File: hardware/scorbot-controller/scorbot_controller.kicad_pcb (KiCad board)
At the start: 2 copper layers, 185 x 128 mm, 102 parts, among them J1 12V in (CUI PJ-102AH, 2.1 mm), J2 12V in (screw terminal, +/-), J3 E-STOP (NC, in VM line), J4 DD-50 female R/A (robot cable), J5 I2C expansion, J6 Spare TCA9555 I/O, J7 FUSE alt: wire inline 5A fuse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, U1 DROK mini buck, set to 5V, U10 Pololu #4035 DRV8874 (M1), U11 Pololu #4035 DRV8874 (M2), U12 Pololu #4035 DRV8874 (M3), U13 Pololu #4035 DRV8874 (M4), U14 Pololu #4035 DRV8874 (M5), U15 Pololu #4035 DRV8874 (M6), U2 ESP32-DevKitC (WROOM-32D or -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, U5 TCA9555PWR (0x20), U6 ADS1115IDGSR (0x48), U7 ADS1115IDGSR (0x49)

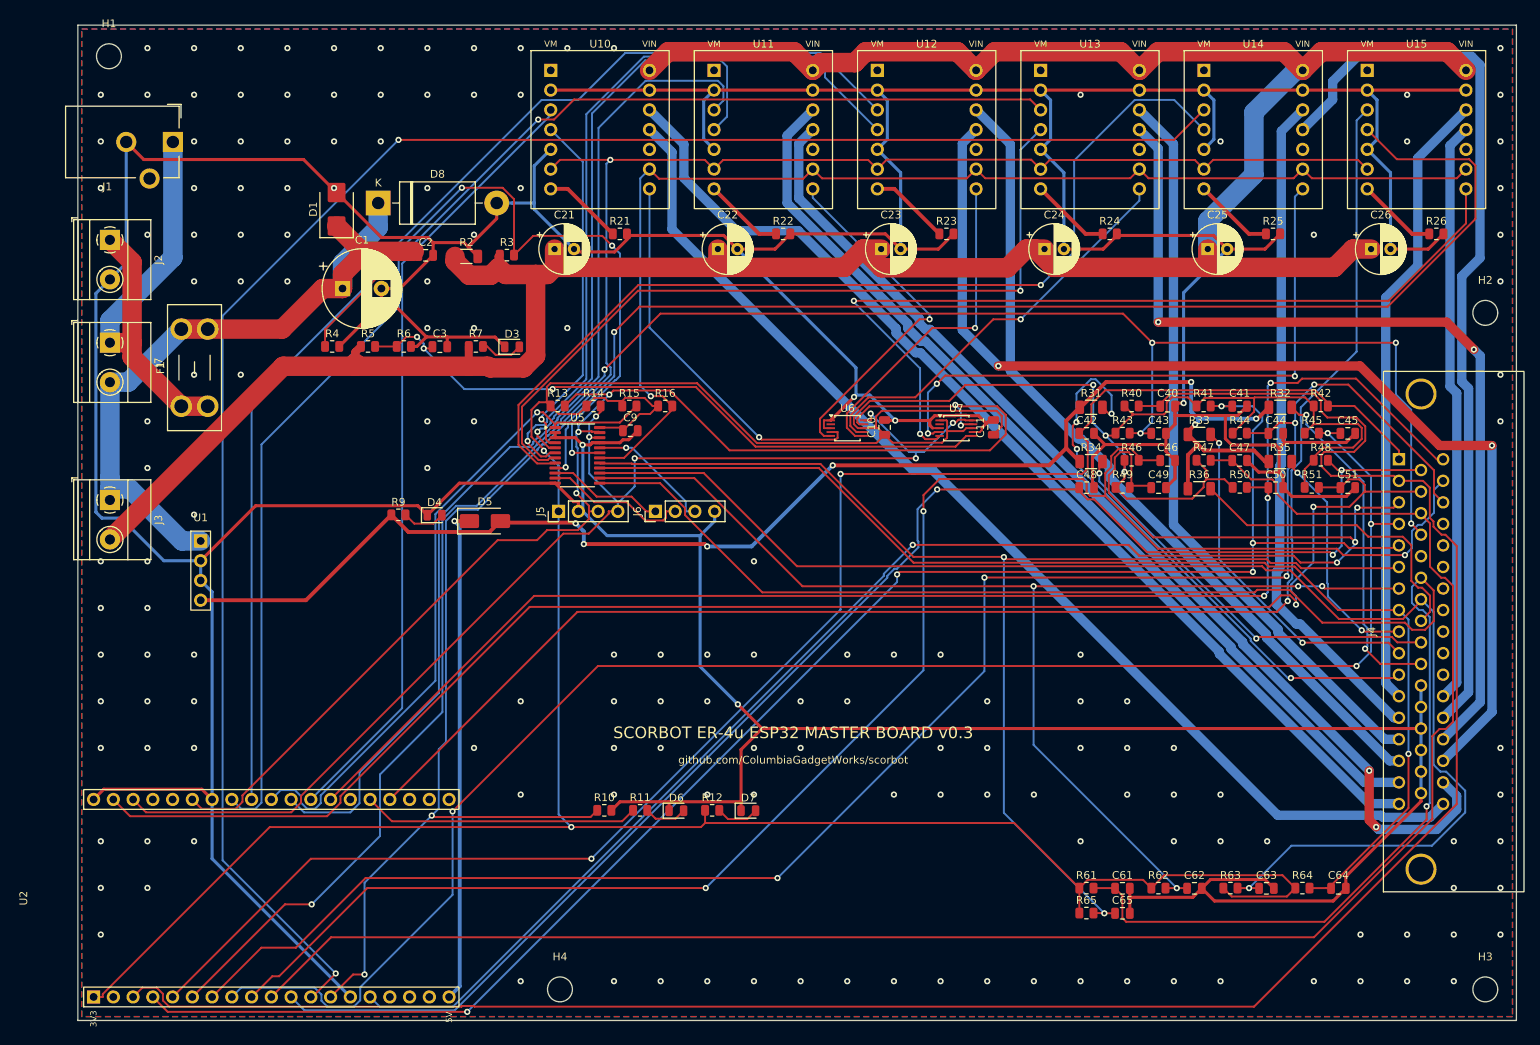
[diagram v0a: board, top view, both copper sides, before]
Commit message: v0.4: DD-50 footprint per Amphenol DD50S564TLF, logos on silkscreen, LCSC fixes
- DD-50: tail rows 2.54 mm apart, row 3 10.40 mm from the flange (Amphenol
  D-Sub brochure, termination type 5); bracket holes still to confirm
- Columbia Gadget Works logo on F.SilkS, Stealie on B.SilkS (silk_art.py)
- R31-R36 47R now 2512 1 W (~0.3 W each); D6 status LED red (C84256)
- Clear LCSC numbers that turned out wrong (TCA9555, 47R); previews draw silk on top

Co-Authored-By: Claude Opus 5.5 <noreply@anthropic.com>
Claude-Session: https://claude.ai/code/session_01EVE6PZ95cMufMkAr9pDFuN
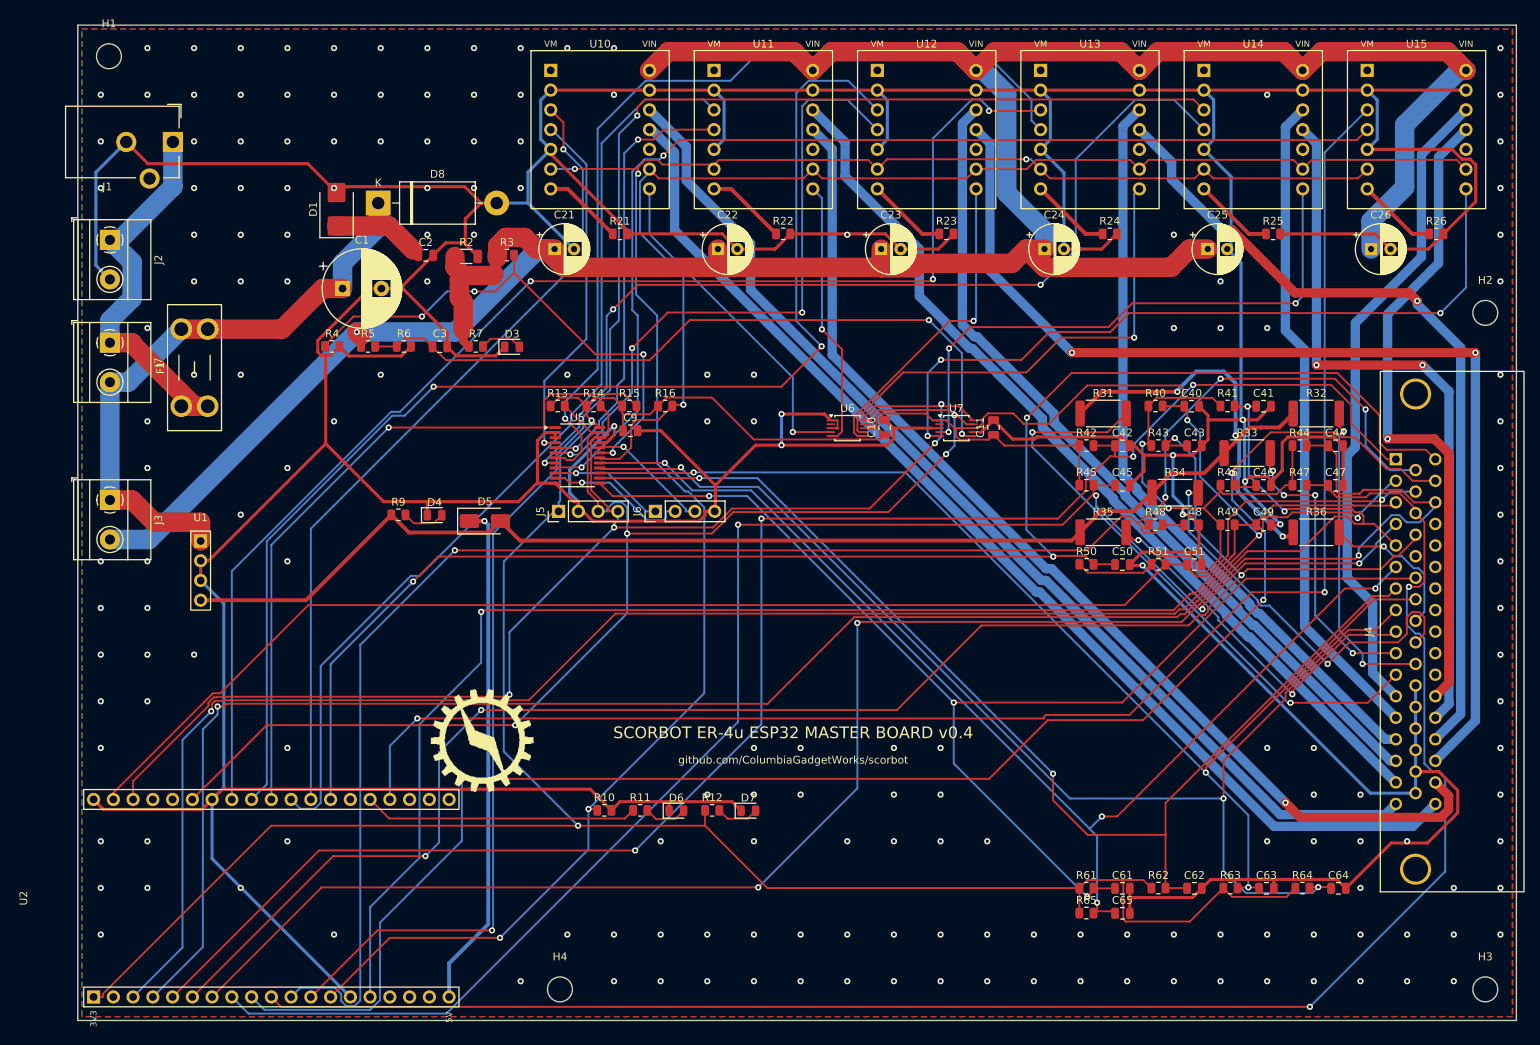
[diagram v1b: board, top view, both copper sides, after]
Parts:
- D6: value STATUS (blue) -> STATUS (red)
- J4: footprint Scorbot:DD50_Female_Horizontal_P2.77x2.84mm -> Scorbot:DD50_Female_Horizontal_P2.77x2.54mm_EdgePinOffset10.40mm
- R31, R32, R33, R34, R35, R36: value 47R 0.25W -> 47R 1W; footprint Resistor_SMD:R_1206_3216Metric -> Resistor_SMD:R_2512_6332Metric
- moved R42 30.6 mm to (159.7, 84.1)
- moved C45 29.7 mm to (164.3, 89.2)
- moved R45 29.7 mm to (159.7, 89.2)
- moved R35 24.5 mm to (161.8, 95.2)
- moved R48 22.8 mm to (168.6, 94.2)
- moved C51 22.1 mm to (173.6, 99.4)
- moved C50 22.1 mm to (164.3, 99.4)
- moved R50 22.1 mm to (159.7, 99.3)
- moved R51 22.1 mm to (169.0, 99.3)
- moved R36 16.0 mm to (189.3, 95.2)
- moved C48 14.3 mm to (173.2, 94.3)
- moved R49 14.3 mm to (177.9, 94.2)
- moved C49 14.3 mm to (182.5, 94.3)
- moved C47 12.7 mm to (191.7, 89.2)
- moved R47 12.7 mm to (187.1, 89.2)
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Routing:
- net ENC1_P0: track 282.8 -> 231.0 mm, vias 0 -> 4
- net SW1: track 207.3 -> 159.6 mm, vias 1 -> 3
- net ENC2_P1: track 253.8 -> 214.8 mm, vias 6 -> 4
- net GND: track 1036.6 -> 1074.3 mm, vias 163 -> 182
- net +3V3: track 491.5 -> 455.7 mm, vias 5 -> 4
- net ENC5_P0: track 193.3 -> 227.2 mm, vias 3 -> 4
- net ENC5_P1: track 213.0 -> 181.3 mm, vias 4 -> 1
- net SW3: track 179.4 -> 150.4 mm, vias 1 -> 3
- net MOT5_B: track 115.2 -> 92.1 mm, vias 0 -> 2
- net VM_SENSE: track 90.0 -> 67.6 mm
- net PH2: track 77.0 -> 56.1 mm, vias 1 -> 2
- net ENC6_VLED: track 40.3 -> 19.6 mm, vias 0 -> 1
- net ENC1_P1: track 214.5 -> 234.0 mm, vias 5 -> 3
- net PH6: track 160.9 -> 141.5 mm
- net PWM5: track 232.2 -> 214.3 mm
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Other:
- board text added: "SCORBOT ER-4u ESP32 MASTER BOARD v0.4"
- board text removed: "SCORBOT ER-4u ESP32 MASTER BOARD v0.3"
